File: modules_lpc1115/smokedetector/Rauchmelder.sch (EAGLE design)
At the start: 75 parts, among them IC1 BD9G101, IC2 LPC1115, Q1 BC856, Q3 BCP52, Q4 ASFL, T1 BC847C, T2 BC817

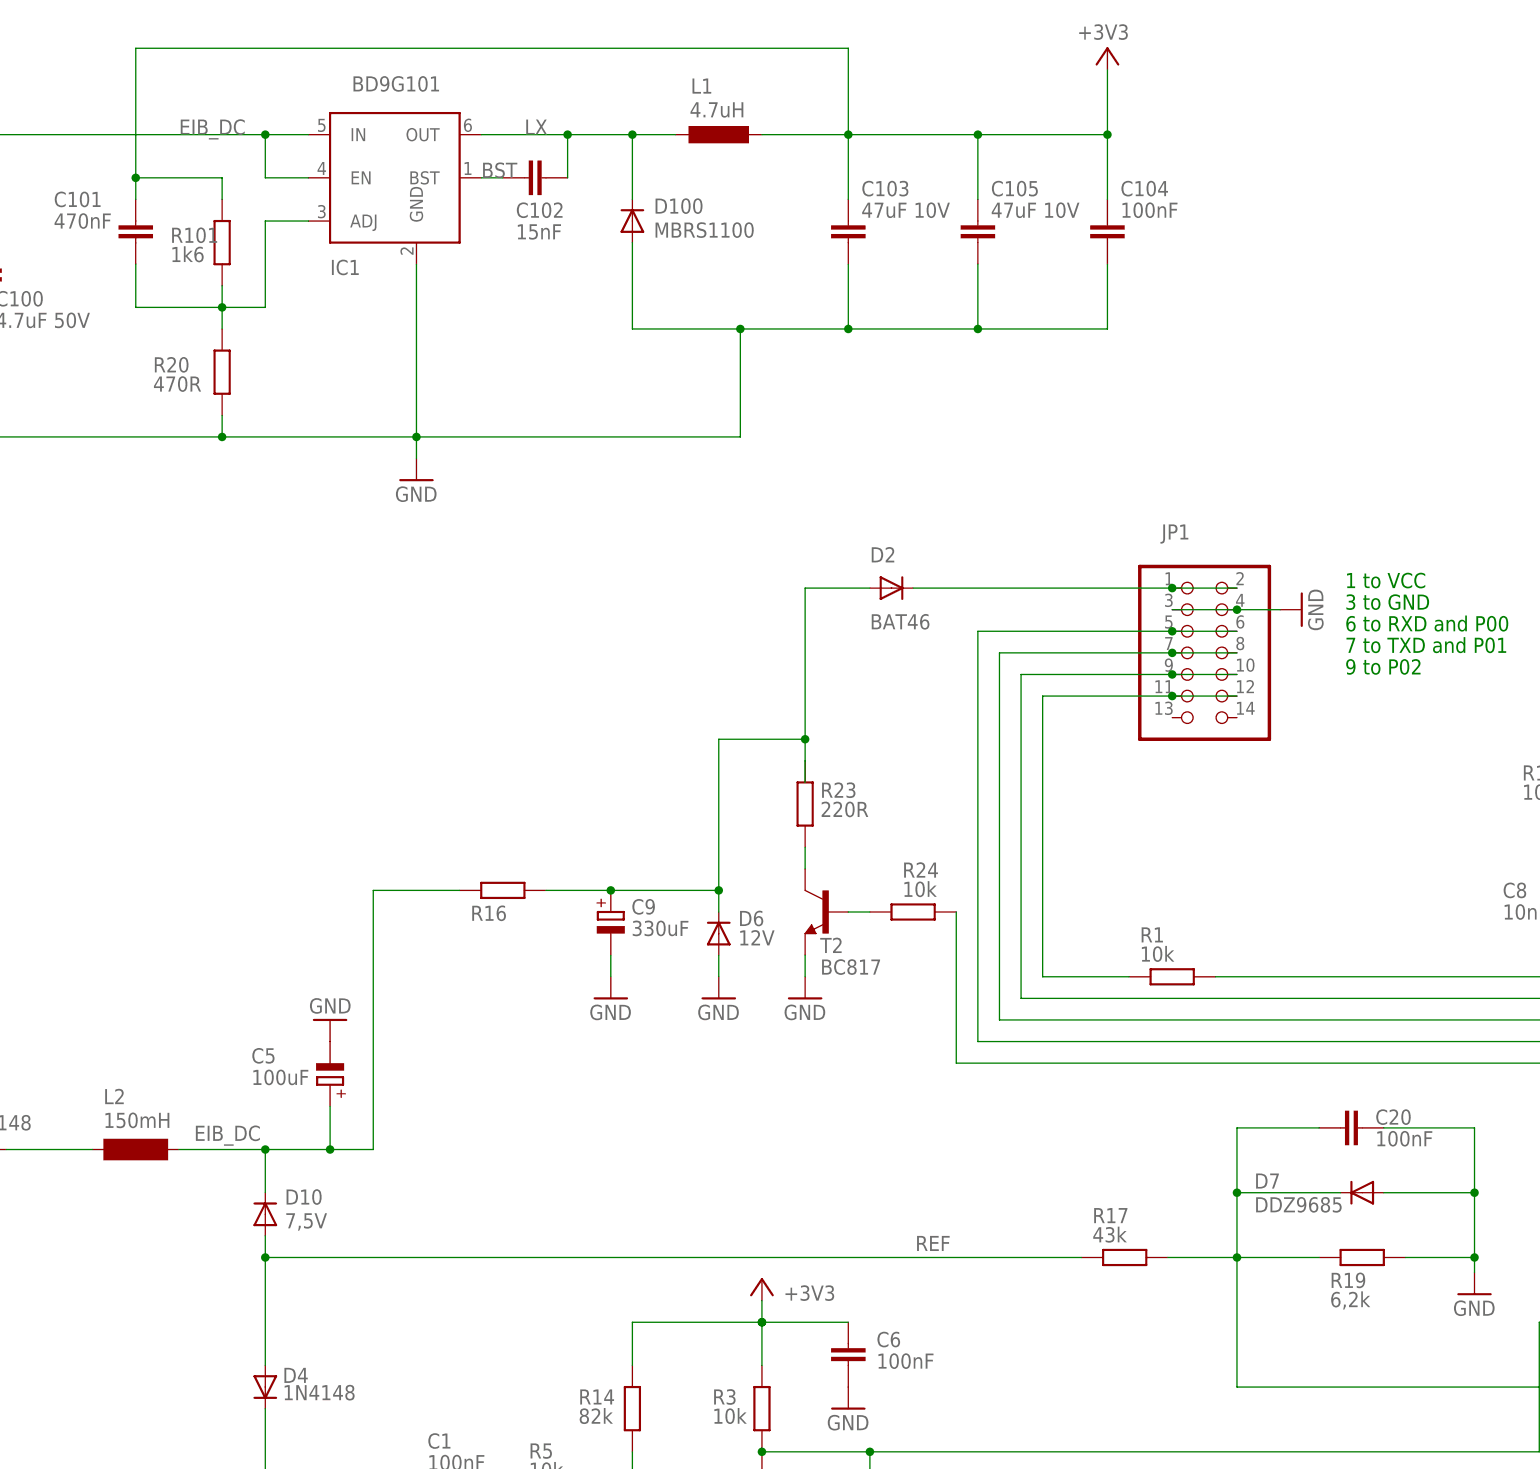
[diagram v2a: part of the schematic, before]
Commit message: [RM] - optimized silk screen; renamed pwr parts to correspond ARM TS
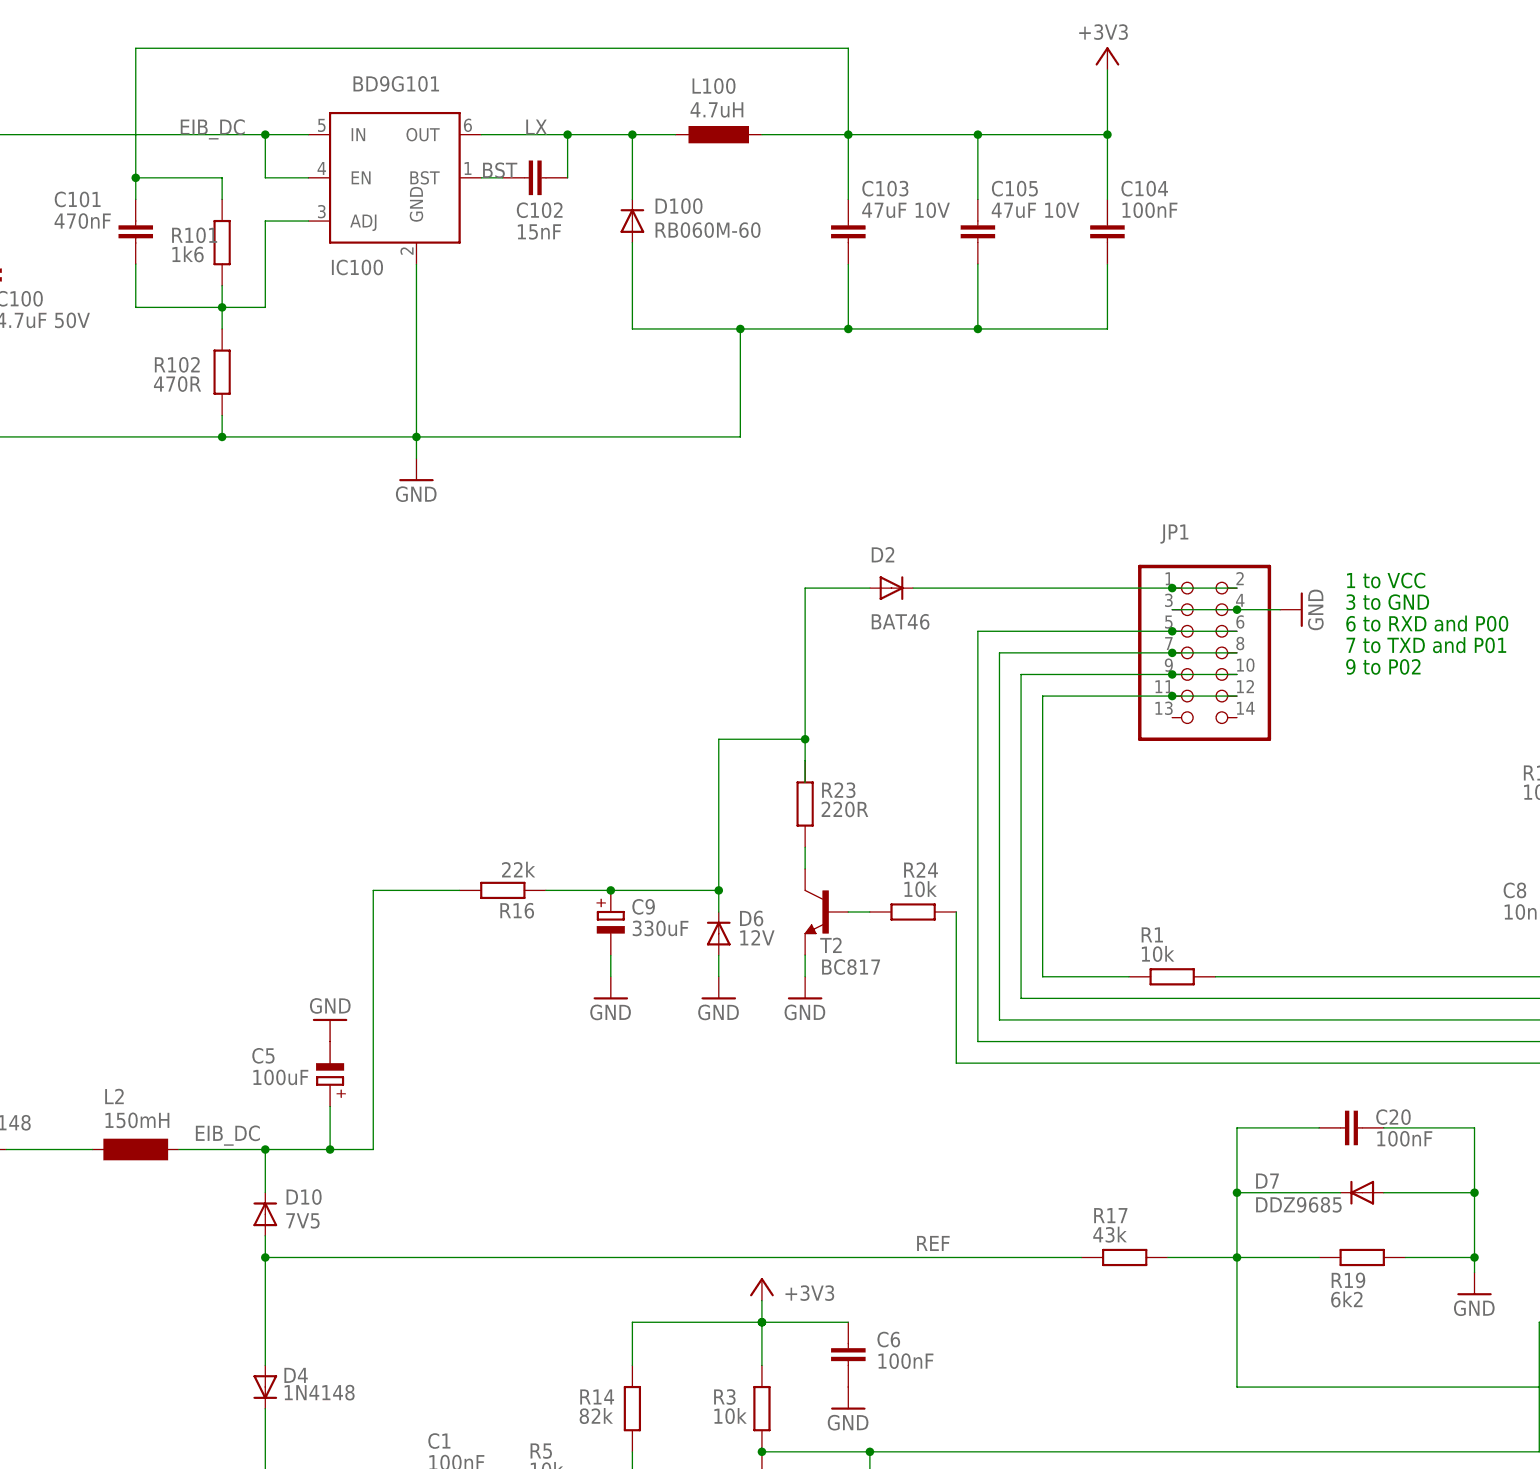
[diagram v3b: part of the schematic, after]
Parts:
- D10: value 7,5V -> 7V5
- D100: value MBRS1100 -> RB060M-60
- R19: value 6,2k -> 6k2
- renumbered IC1 to IC100, L1 to L100, R20 to R102
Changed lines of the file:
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@@
 <part name="Q1" library="transistor-pnp" deviceset="BC856*" device="SMD" technology="ALT1" value="BC856"/>
 <part name="T1" library="transistor" deviceset="BC847C" device=""/>
-<part name="D10" library="microbuilder" deviceset="DIODE" device="SOD-123" value="7,5V"/>
+<part name="D10" library="microbuilder" deviceset="DIODE" device="SOD-123" value="7V5"/>
 <part name="D6" library="microbuilder" deviceset="DIODE" device="SOD-123" value="12V"/>
 <part name="C5" library="rcl" library_urn="urn:adsk.eagle:library:334" deviceset="CPOL-EU" device="SANYO_SMD_C6" package3d_urn="urn:adsk.eagle:package:23465/1" value="100uF"/>
@@
 <part name="GND1" library="supply1" deviceset="GND" device=""/>
 <part name="R17" library="rcl" library_urn="urn:adsk.eagle:library:334" deviceset="R-EU_" device="R0805" package3d_urn="urn:adsk.eagle:package:23553/2" value="43k"/>
-<part name="R19" library="rcl" library_urn="urn:adsk.eagle:library:334" deviceset="R-EU_" device="R0805" package3d_urn="urn:adsk.eagle:package:23553/2" value="6,2k"/>
+<part name="R19" library="rcl" library_urn="urn:adsk.eagle:library:334" deviceset="R-EU_" device="R0805" package3d_urn="urn:adsk.eagle:package:23553/2" value="6k2"/>
 <part name="D7" library="microbuilder" deviceset="DIODE" device="SOD-123" value="DDZ9685">
 <attribute name="ALTERNATIVE" value="MMSZ4684T1G"/>
@@
 <part name="C104" library="rcl" library_urn="urn:adsk.eagle:library:334" deviceset="C-EU" device="C0805" package3d_urn="urn:adsk.eagle:package:23617/2" value="100nF"/>
 <part name="P+2" library="supply1" deviceset="+3V3" device=""/>
-<part name="IC1" library="Stefan_selfbus" deviceset="BD9G101G" device="BD9G101G-SOT23-6" value="BD9G101"/>
-<part name="L1" library="rcl_changed" deviceset="L-EU" device="L4532P" package3d_urn="urn:adsk.eagle:package:23484/1" value="4.7uH"/>
+<part name="IC100" library="Stefan_selfbus" deviceset="BD9G101G" device="BD9G101G-SOT23-6" value="BD9G101"/>
+<part name="L100" library="rcl_changed" deviceset="L-EU" device="L4532P" package3d_urn="urn:adsk.eagle:package:23484/1" value="4.7uH"/>
 <part name="C100" library="rcl" library_urn="urn:adsk.eagle:library:334" deviceset="C-EU" device="C0805" package3d_urn="urn:adsk.eagle:package:23617/2" value="4.7uF 50V"/>
 <part name="C103" library="rcl" library_urn="urn:adsk.eagle:library:334" deviceset="C-EU" device="C0805" package3d_urn="urn:adsk.eagle:package:23617/2" value="47uF 10V"/>
 <part name="C102" library="rcl" library_urn="urn:adsk.eagle:library:334" deviceset="C-EU" device="C0805" package3d_urn="urn:adsk.eagle:package:23617/2" value="15nF"/>
 <part name="R101" library="rcl" library_urn="urn:adsk.eagle:library:334" deviceset="R-EU_" device="R0805" package3d_urn="urn:adsk.eagle:package:23553/2" value="1k6"/>
-<part name="R20" library="rcl" library_urn="urn:adsk.eagle:library:334" deviceset="R-EU_" device="R0805" package3d_urn="urn:adsk.eagle:package:23553/2" value="470R"/>
+<part name="R102" library="rcl" library_urn="urn:adsk.eagle:library:334" deviceset="R-EU_" device="R0805" package3d_urn="urn:adsk.eagle:package:23553/2" value="470R"/>
 <part name="C101" library="rcl" library_urn="urn:adsk.eagle:library:334" deviceset="C-EU" device="C0805" package3d_urn="urn:adsk.eagle:package:23617/2" value="470nF"/>
-<part name="D100" library="microbuilder" deviceset="DIODE" device="SOD-123" value="MBRS1100"/>
+<part name="D100" library="microbuilder" deviceset="DIODE" device="SOD-123" value="RB060M-60"/>
 <part name="FD1" library="Fiducial" deviceset="FID" device="_40MIL" value="FID_40MIL"/>
 <part name="FD2" library="Fiducial" deviceset="FID" device="_40MIL" value="FID_40MIL"/>
@@
 </instance>
 <instance part="R16" gate="G$1" x="93.98" y="134.62" smashed="yes" rot="R180">
-<attribute name="NAME" x="90.17" y="131.0386" size="1.778" layer="95"/>
+<attribute name="NAME" x="97.79" y="133.1214" size="1.778" layer="95" rot="R180"/>
+<attribute name="VALUE" x="97.79" y="137.922" size="1.778" layer="96" rot="R180"/>
 </instance>
 <instance part="C9" gate="G$1" x="106.68" y="132.08" smashed="yes">
@@
 <attribute name="VALUE" x="161.544" y="234.696" size="1.778" layer="96"/>
 </instance>
-<instance part="IC1" gate="G$1" x="81.28" y="218.44" smashed="yes">
+<instance part="IC100" gate="G$1" x="81.28" y="218.44" smashed="yes">
 <attribute name="NAME" x="73.66" y="207.01" size="1.778" layer="95"/>
 <attribute name="VALUE" x="76.2" y="228.6" size="1.778" layer="96"/>
 </instance>
-<instance part="L1" gate="G$1" x="119.38" y="223.52" smashed="yes" rot="R90">
+<instance part="L100" gate="G$1" x="119.38" y="223.52" smashed="yes" rot="R90">
 <attribute name="NAME" x="116.078" y="228.346" size="1.778" layer="95"/>
 <attribute name="VALUE" x="115.951" y="225.552" size="1.778" layer="96"/>
@@
 <attribute name="VALUE" x="54.864" y="208.534" size="1.778" layer="96"/>
 </instance>
-<instance part="R20" gate="G$1" x="60.96" y="195.58" smashed="yes" rot="R90">
+<instance part="R102" gate="G$1" x="60.96" y="195.58" smashed="yes" rot="R90">
 <attribute name="NAME" x="52.832" y="195.5546" size="1.778" layer="95"/>
 <attribute name="VALUE" x="52.832" y="193.294" size="1.778" layer="96"/>
@@
 <segment>
 <pinref part="GND16" gate="1" pin="GND"/>
-<pinref part="IC1" gate="G$1" pin="GND"/>
+<pinref part="IC100" gate="G$1" pin="GND"/>
 <wire x1="83.82" y1="185.42" x2="83.82" y2="187.96" width="0.1524" layer="91"/>
 <wire x1="83.82" y1="187.96" x2="83.82" y2="208.28" width="0.1524" layer="91"/>
-<pinref part="R20" gate="G$1" pin="1"/>
+<pinref part="R102" gate="G$1" pin="1"/>
 <wire x1="33.02" y1="187.96" x2="60.96" y2="187.96" width="0.1524" layer="91"/>
 <wire x1="60.96" y1="187.96" x2="83.82" y2="187.96" width="0.1524" layer="91"/>
@@
 </segment>
 <segment>
-<pinref part="IC1" gate="G$1" pin="IN"/>
+<pinref part="IC100" gate="G$1" pin="IN"/>
 <wire x1="66.04" y1="223.52" x2="71.12" y2="223.52" width="0.1524" layer="91"/>
 <junction x="66.04" y="223.52"/>
@@
 <label x="55.88" y="223.52" size="1.778" layer="95"/>
 <wire x1="66.04" y1="223.52" x2="66.04" y2="218.44" width="0.1524" layer="91"/>
-<pinref part="IC1" gate="G$1" pin="EN"/>
+<pinref part="IC100" gate="G$1" pin="EN"/>
 <wire x1="66.04" y1="218.44" x2="71.12" y2="218.44" width="0.1524" layer="91"/>
 </segment>
@@
 <net name="LX" class="0">
 <segment>
-<pinref part="IC1" gate="G$1" pin="OUT"/>
+<pinref part="IC100" gate="G$1" pin="OUT"/>
 <wire x1="91.44" y1="223.52" x2="101.6" y2="223.52" width="0.1524" layer="91"/>
 <pinref part="C102" gate="G$1" pin="1"/>
@@
 <wire x1="109.22" y1="223.52" x2="114.3" y2="223.52" width="0.1524" layer="91"/>
 <wire x1="101.6" y1="218.44" x2="101.6" y2="223.52" width="0.1524" layer="91"/>
-<pinref part="L1" gate="G$1" pin="1"/>
+<pinref part="L100" gate="G$1" pin="1"/>
 <wire x1="109.22" y1="215.9" x2="109.22" y2="223.52" width="0.1524" layer="91"/>
 <junction x="101.6" y="223.52"/>
@@
 <segment>
 <pinref part="C102" gate="G$1" pin="2"/>
-<pinref part="IC1" gate="G$1" pin="BST"/>
+<pinref part="IC100" gate="G$1" pin="BST"/>
 <wire x1="93.98" y1="218.44" x2="91.44" y2="218.44" width="0.1524" layer="91"/>
 <label x="91.44" y="218.44" size="1.778" layer="95"/>
@@
 <net name="FB1" class="0">
 <segment>
-<pinref part="IC1" gate="G$1" pin="ADJ"/>
+<pinref part="IC100" gate="G$1" pin="ADJ"/>
 <wire x1="71.12" y1="213.36" x2="66.04" y2="213.36" width="0.1524" layer="91"/>
 <pinref part="C101" gate="G$1" pin="1"/>
 <wire x1="50.8" y1="208.28" x2="50.8" y2="203.2" width="0.1524" layer="91"/>
-<pinref part="R20" gate="G$1" pin="2"/>
+<pinref part="R102" gate="G$1" pin="2"/>
 <wire x1="50.8" y1="203.2" x2="60.96" y2="203.2" width="0.1524" layer="91"/>
 <pinref part="R101" gate="G$1" pin="1"/>
@@
 <pinref part="C103" gate="G$1" pin="1"/>
 <wire x1="134.62" y1="223.52" x2="134.62" y2="215.9" width="0.1524" layer="91"/>
-<pinref part="L1" gate="G$1" pin="2"/>
+<pinref part="L100" gate="G$1" pin="2"/>
 <wire x1="134.62" y1="223.52" x2="124.46" y2="223.52" width="0.1524" layer="91"/>
 <pinref part="C105" gate="G$1" pin="1"/>
